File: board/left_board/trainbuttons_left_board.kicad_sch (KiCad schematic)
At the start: 4 parts, among them J101 USB_C_Receptacle_USB2.0_16P, J102 HDMI_A

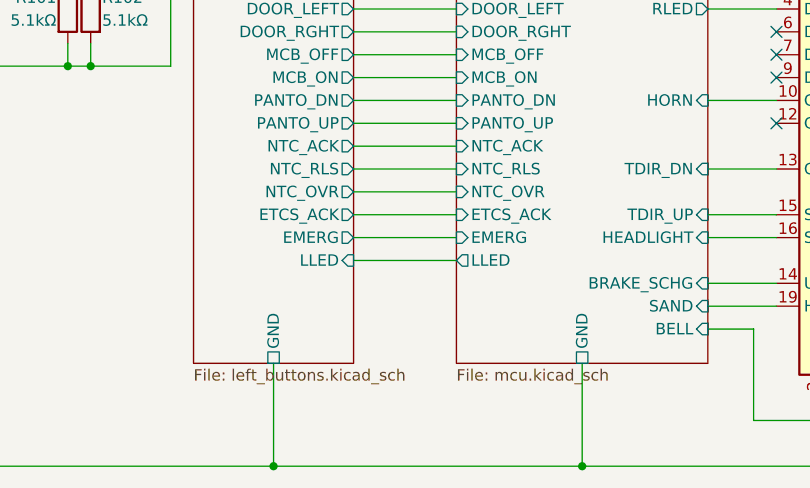
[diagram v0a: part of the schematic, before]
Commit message: add support for pedal
the pedal is mostly envisioned as a secondary dead man's switch input, but
to enable flexible usage, it is wired up to the µC's ADC and supplies
12-bit values for the X axis

things will be set up to cooperate with a Brother-compatible sewing machine
pedal because that's what I have lying around -- those that connect using a
3.5mm TS phone connector, nothing even close to mains voltage
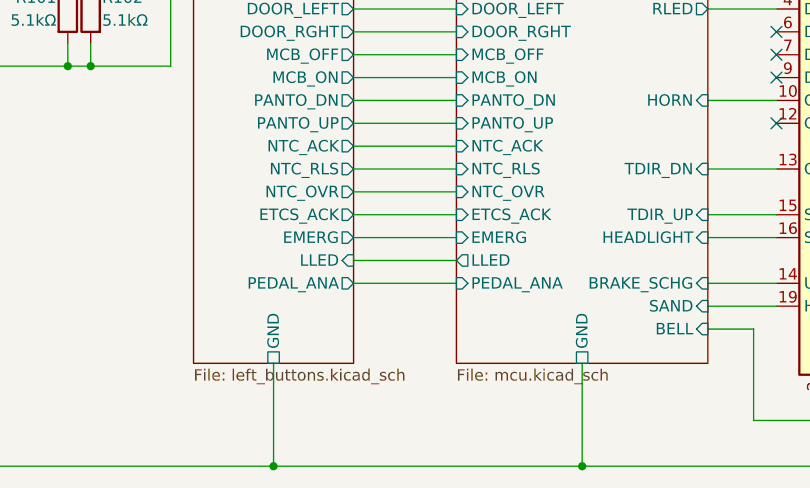
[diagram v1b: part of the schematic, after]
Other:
- sheet Left Buttons ports: added PEDAL_ANA; removed none
- sheet MCU ports: added PEDAL_ANA; removed none
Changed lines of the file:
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@@
+	(wire
+		(pts
+			(xy 82.55 90.17) (xy 93.98 90.17)
+		)
+		(stroke
+			(width 0)
+			(type default)
+		)
+	)
 	(wire
 		(pts
@@
 			)
 		)
+		(pin "PEDAL_ANA" input
+			(at 93.98 90.17 180)
+			(effects
+				(font
+					(size 1.27 1.27)
+				)
+				(justify left)
+			)
+		)
 		(instances
 			(project "trainbuttons_left_board"
@@
 			(effects
 				(font
+					(size 1.27 1.27)
+				)
+				(justify right)
+			)
+		)
+		(pin "PEDAL_ANA" output
+			(at 82.55 90.17 0)
+			(effects
+				(font
